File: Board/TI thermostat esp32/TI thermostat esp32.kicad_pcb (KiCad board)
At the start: 2 copper layers, 173 x 73.6 mm, 91 parts, among them IC1 ESP32-WROVER-E_M213EH6464PH3Q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, IC2 LT1074CT, J1 bme280, J4 Conn_02x05_Odd_Even, J5 Conn_02x03_Odd_Even, J6 Conn_01x08, Q1 BT134-600, Q2 BT134-600, Q3 BT134-600, Q4 BT134-600, SW1 SW_Push, U1 MOC3063M, U2 MOC3063M, U3 MOC3063M, U4 MOC3063M, U5 74HC00, U6 MAX7219, U7 74HC00, U8 LD1117S33TR_SOT223, U9 74HC138

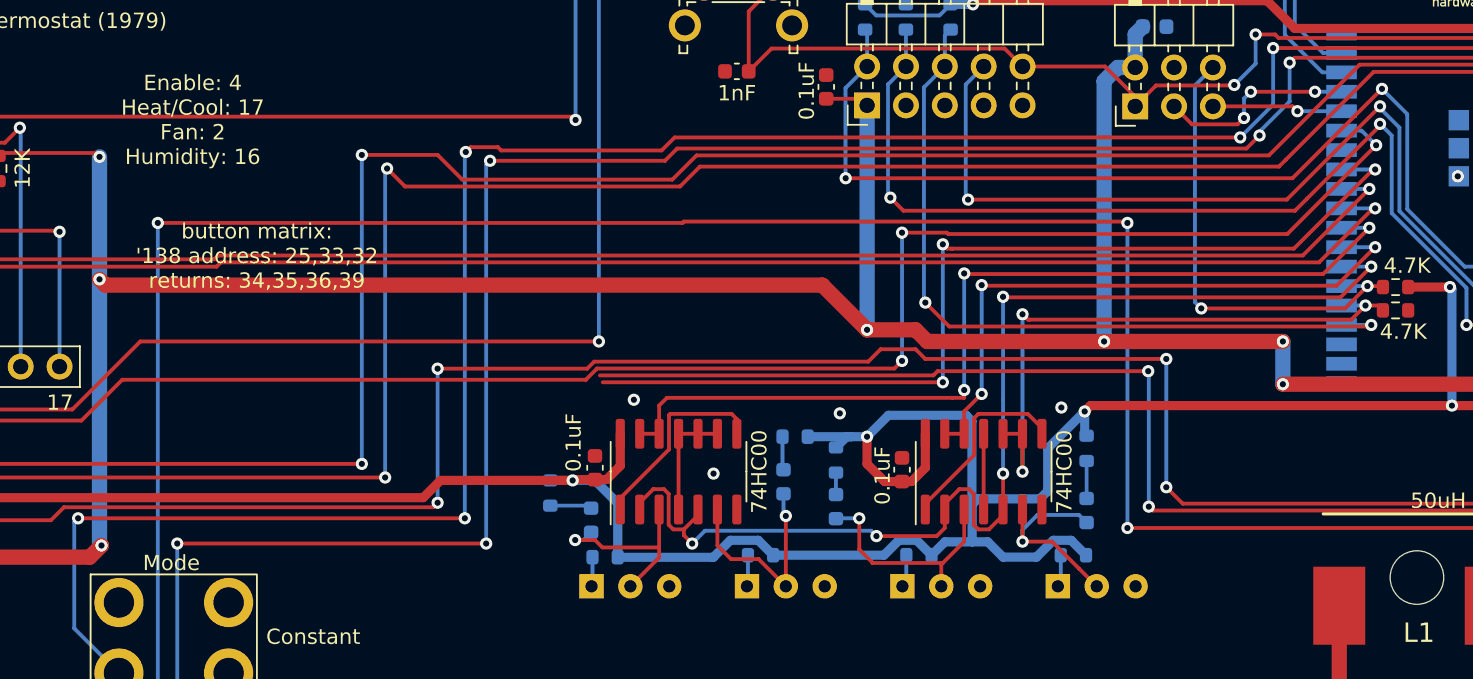
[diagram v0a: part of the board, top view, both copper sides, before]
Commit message: rev2 pcb and layout plus test code
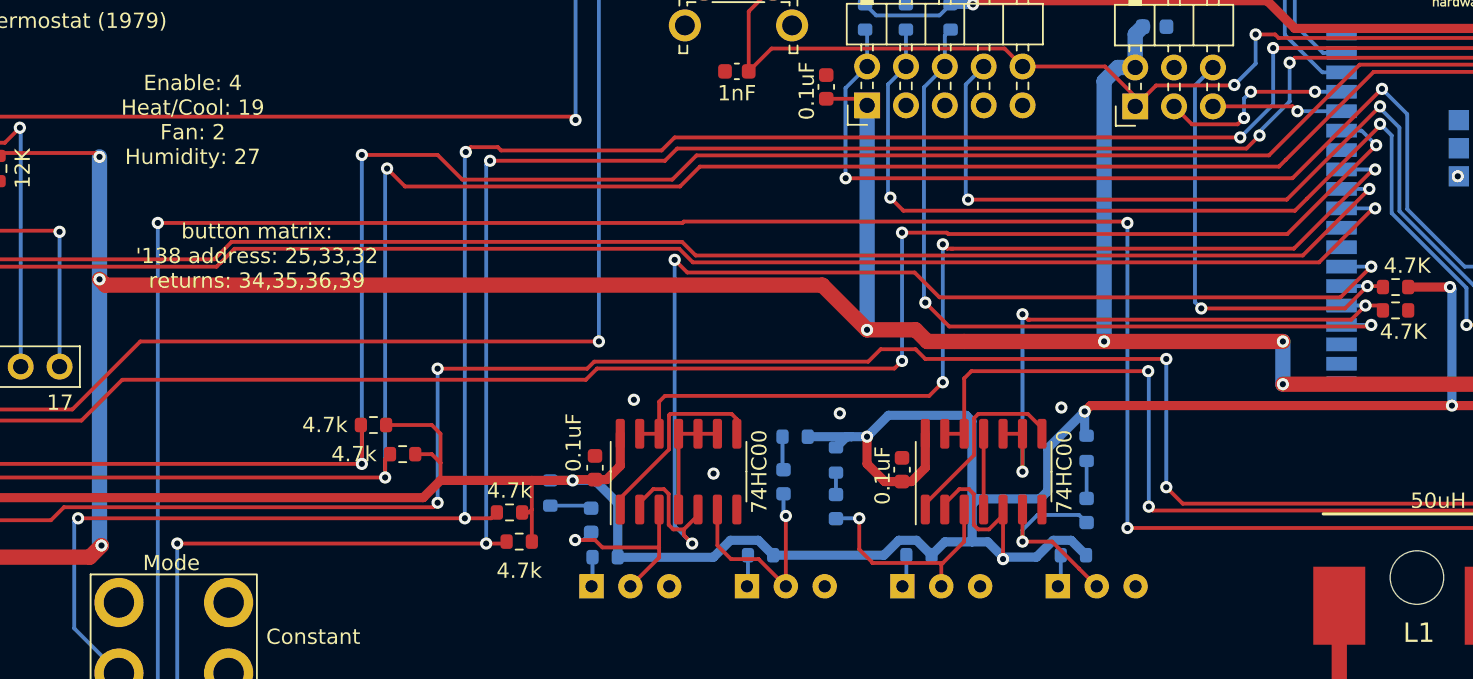
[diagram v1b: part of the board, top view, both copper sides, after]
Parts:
- added R16: 4.7k, Resistor_SMD:R_0603_1608Metric, F.Cu at (138.4, 95.9)
- added R17: 4.7k, Resistor_SMD:R_0603_1608Metric, F.Cu at (128.9, 88.3)
- added R19: 4.7k, Resistor_SMD:R_0603_1608Metric, F.Cu at (130.8, 90.2)
- added R21: 4.7k, Resistor_SMD:R_0603_1608Metric, F.Cu at (137.8, 94.0)
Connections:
- IC1 pad 27: /ESP_IO16 -> unconnected-(IC1-Pad27)
- IC1 pad 28: /ESP_IO17 -> unconnected-(IC1-Pad28)
- U5 pad 12: /ESP_IO16 -> /ESP_IO27
- U5 pad 13: /ESP_IO16 -> /ESP_IO27
- U5 pad 2: /ESP_IO4 -> +3V3
- U5 pad 5: /ESP_IO4 -> +3V3
- U7 pad 12: /ESP_IO17 -> /ESP_IO19
- U7 pad 13: /ESP_IO17 -> /ESP_IO19
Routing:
- net /ESP_IO17: track 60.8 -> 0.00 mm, vias 3 -> 0
- net /ESP_IO16: track 40.2 -> 0.00 mm, vias 3 -> 0
- net +3V3: track 353.9 -> 378.2 mm, vias 10 -> 11
- net /ESP_IO27: track 90.9 -> 72.1 mm
- net /ESP_IO34: track 227.6 -> 230.2 mm
- net /ESP_IO36: track 157.9 -> 160.1 mm
- net /ESP_IO35: track 246.6 -> 248.3 mm
- net /ESP_IO4: track 75.6 -> 77.1 mm, vias 5 -> 3
- net /ESP_IO39: track 169.9 -> 171.2 mm
- net /ESP_IO5: track 115.8 -> 116.5 mm
- net /ESP_IO18: track 105.7 -> 106.4 mm
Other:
- board text added: "Enable: 4 Heat/Cool: 19 Fan: 2 Humidity: 27"
- board text added: "Rev. 2"
- board text removed: "Enable: 4 Heat/Cool: 17 Fan: 2 Humidity: 16"
